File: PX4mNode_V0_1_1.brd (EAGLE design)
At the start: 48.6 x 34.9 mm, 140 parts, among them J201 DF13C-6P-1.25V, J202 DF13C-6P-1.25V, J203 DF13C-6P-1.25V, J301 DF13C-4P-1.25V, J401 DF13C-7P-1.25V, J402 DF13-4P-1.25V, J403 DF13C-4P-1.25V, J404 DF13C-4P-1.25V, J405 DF13C-4P-1.25V, J801 DF13C-3P-1.25V, M3_MOUNT1101 MOUNT-HOLE3.1MM, M3_MOUNT1102 MOUNT-HOLE3.1MM, M3_MOUNT1103 MOUNT-HOLE3.1MM, M3_MOUNT1104 MOUNT-HOLE3.1MM, U101 STM32F4X7VX, U401 MAX3051, U402 MAX3051, X101 3.2x2.5 mm / 24 MHz / 15 ppm

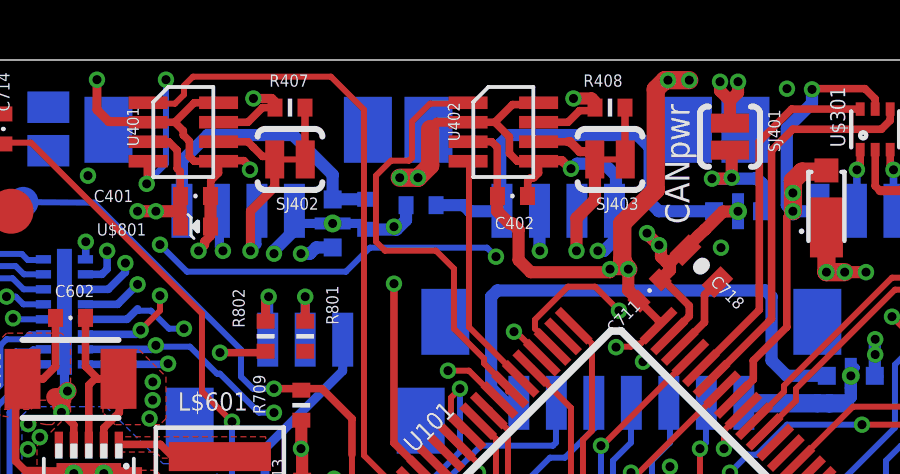
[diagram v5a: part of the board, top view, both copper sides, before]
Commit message: Stop mask removed from vias
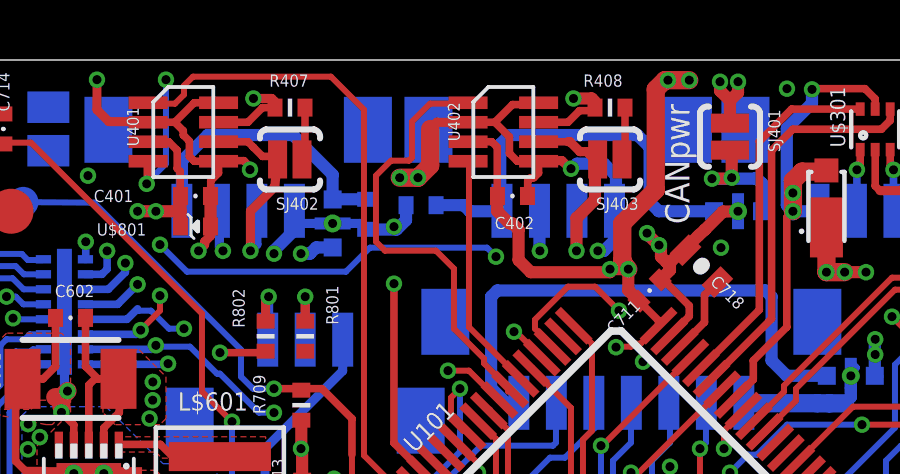
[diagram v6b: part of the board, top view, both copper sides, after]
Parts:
- SJ402, SJ403: value SOLDERJUMPERTRACE -> SOLDERJUMPERNC2; device SparkFun-Passives:SJ_2S-TRACE -> SparkFun-Passives:SJ_2S-NOTRACE
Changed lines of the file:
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@@
 <grid distance="0.1" unitdist="mm" unit="mm" style="dots" multiple="1" display="yes" altdistance="4" altunitdist="mil" altunit="mm"/>
 <layers>
-<layer number="1" name="Top" color="4" fill="1" visible="no" active="yes"/>
+<layer number="1" name="Top" color="4" fill="1" visible="yes" active="yes"/>
 <layer number="2" name="Ground" color="2" fill="10" visible="no" active="yes"/>
 <layer number="3" name="Horizontal" color="13" fill="15" visible="no" active="yes"/>
@@
 <layer number="13" name="Route13" color="4" fill="5" visible="no" active="no"/>
 <layer number="14" name="Vertical" color="14" fill="15" visible="no" active="yes"/>
-<layer number="15" name="Power" color="11" fill="15" visible="yes" active="yes"/>
-<layer number="16" name="Bottom" color="1" fill="1" visible="no" active="yes"/>
+<layer number="15" name="Power" color="11" fill="15" visible="no" active="yes"/>
+<layer number="16" name="Bottom" color="1" fill="1" visible="yes" active="yes"/>
 <layer number="17" name="Pads" color="2" fill="1" visible="yes" active="yes"/>
 <layer number="18" name="Vias" color="2" fill="1" visible="yes" active="yes"/>
-<layer number="19" name="Unrouted" color="14" fill="1" visible="yes" active="yes"/>
+<layer number="19" name="Unrouted" color="14" fill="1" visible="no" active="yes"/>
 <layer number="20" name="Dimension" color="15" fill="1" visible="yes" active="yes"/>
 <layer number="21" name="tPlace" color="7" fill="1" visible="yes" active="yes"/>
@@
 <layer number="27" name="tValues" color="7" fill="1" visible="no" active="yes"/>
 <layer number="28" name="bValues" color="7" fill="1" visible="no" active="yes"/>
-<layer number="29" name="tStop" color="7" fill="3" visible="no" active="yes"/>
+<layer number="29" name="tStop" color="7" fill="3" visible="yes" active="yes"/>
 <layer number="30" name="bStop" color="7" fill="6" visible="no" active="yes"/>
-<layer number="31" name="tCream" color="7" fill="4" visible="no" active="yes"/>
+<layer number="31" name="tCream" color="7" fill="4" visible="yes" active="yes"/>
 <layer number="32" name="bCream" color="7" fill="5" visible="no" active="yes"/>
 <layer number="33" name="tFinish" color="6" fill="3" visible="no" active="yes"/>
@@
 <param name="mlMinCreamFrame" value="0mil"/>
 <param name="mlMaxCreamFrame" value="0.2mm"/>
-<param name="mlViaStopLimit" value="0mil"/>
+<param name="mlViaStopLimit" value="0.31mm"/>
 <param name="srRoundness" value="0"/>
 <param name="srMinRoundness" value="0mil"/>
@@
 </element>
 <element name="L402" library="PX4lite" package="DFN16-THIN" value="NUF8402MN" x="49.9872" y="23.5712" rot="MR90"/>
-<element name="SJ403" library="SparkFun-Passives" package="SJ_2S-TRACE" value="SOLDERJUMPERTRACE" x="38.2016" y="34.3408" rot="R180"/>
+<element name="SJ403" library="SparkFun-Passives" package="SJ_2S-NOTRACE" value="SOLDERJUMPERNC2" x="38.2016" y="34.3408" rot="R180"/>
 <element name="J$401" library="PX4lite" package="HEADER_3X01_SMD_H_BOARD_EDGE_SHORT" value="HEADER-3X1BOARDEDGE-SHORT" x="45.6" y="3.9624" smashed="yes" rot="R180">
 <attribute name="NAME" x="52.0324" y="4.19" size="0.6096" layer="25" font="vector" ratio="15" rot="R180"/>
@@
 <attribute name="PARTNO" value="PESD0402-140" x="34.9504" y="34.7472" size="1.778" layer="28" rot="MR270" display="off"/>
 </element>
-<element name="SJ402" library="SparkFun-Passives" package="SJ_2S-TRACE" value="SOLDERJUMPERTRACE" x="27.5336" y="34.3408" rot="R180"/>
+<element name="SJ402" library="SparkFun-Passives" package="SJ_2S-NOTRACE" value="SOLDERJUMPERNC2" x="27.5336" y="34.3408" rot="R180"/>
 <element name="U$501" library="PX4lite" package="16LGA-3X3" value="MAX21100" x="49.276" y="9.7536" smashed="yes">
 <attribute name="NAME" x="48.376" y="7.2536" size="0.5" layer="25" font="vector" ratio="15"/>
@@
 <wire x1="37.084" y1="32.384" x2="37.7" y2="33" width="0.4064" layer="1"/>
 <wire x1="37.7" y1="33" x2="37.7" y2="34.3344" width="0.4064" layer="1"/>
-<wire x1="37.7" y1="34.3344" x2="37.6936" y2="34.3408" width="0.4064" layer="1"/>
+<wire x1="37.7" y1="34.3344" x2="37.7889" y2="34.3408" width="0.4064" layer="1"/>
 <wire x1="36.7994" y1="34.9302" x2="36.8698" y2="34.9302" width="0.3048" layer="1"/>
 <wire x1="36.8698" y1="34.9302" x2="37.2" y2="34.6" width="0.3048" layer="1"/>
 <wire x1="37.2" y1="34.6" x2="37.4344" y2="34.6" width="0.3048" layer="1"/>
-<wire x1="37.5344" y1="34.5" x2="37.6936" y2="34.3408" width="0.3048" layer="1"/>
+<wire x1="37.5344" y1="34.5" x2="37.7889" y2="34.3408" width="0.3048" layer="1"/>
 <wire x1="37.4344" y1="34.6" x2="37.5344" y2="34.5" width="0.3048" layer="1"/>
 </signal>
@@
 <vertex x="42.3" y="32.2"/>
 <vertex x="43.7" y="32.2"/>
-<vertex x="43.7" y="32.2"/>
 <vertex x="45.7" y="32.2"/>
 <vertex x="46.8" y="31.1"/>
@@
 <contactref element="SJ403" pad="1"/>
 <wire x1="38.7016" y1="36.068" x2="38.7016" y2="34.3488" width="0.254" layer="1"/>
-<wire x1="38.7016" y1="34.3488" x2="38.7096" y2="34.3408" width="0.254" layer="1"/>
+<wire x1="38.7016" y1="34.3488" x2="38.6025" y2="34.3408" width="0.254" layer="1"/>
 </signal>
 <signal name="N$28" class="1">
@@
 <contactref element="R407" pad="P$2"/>
 <contactref element="SJ402" pad="1"/>
-<wire x1="28.0416" y1="34.3408" x2="28.0336" y2="34.3488" width="0.254" layer="1"/>
+<wire x1="27.9345" y1="34.3408" x2="28.0336" y2="34.3488" width="0.254" layer="1"/>
 <wire x1="28.0336" y1="34.3488" x2="28.0336" y2="36.068" width="0.254" layer="1"/>
 </signal>
@@
 <contactref element="J404" pad="P$3"/>
 <contactref element="SJ402" pad="2"/>
-<wire x1="27.0256" y1="34.3408" x2="26.924" y2="34.4424" width="0.254" layer="1"/>
+<wire x1="27.1209" y1="34.3408" x2="26.924" y2="34.4424" width="0.254" layer="1"/>
 <wire x1="26.924" y1="34.4424" x2="26.616" y2="34.4424" width="0.254" layer="1"/>
 <wire x1="26.616" y1="34.4424" x2="26.3144" y2="34.744" width="0.254" layer="1"/>
@@
 <wire x1="26.216" y1="31.2928" x2="26.216" y2="32.6168" width="0.3048" layer="1"/>
 <wire x1="26.216" y1="32.6168" x2="27.0256" y2="33.4264" width="0.3048" layer="1"/>
-<wire x1="27.0256" y1="33.4264" x2="27.0256" y2="34.3408" width="0.3048" layer="1"/>
+<wire x1="27.0256" y1="33.4264" x2="27.1209" y2="34.3408" width="0.3048" layer="1"/>
 </signal>
 <signal name="REGD">

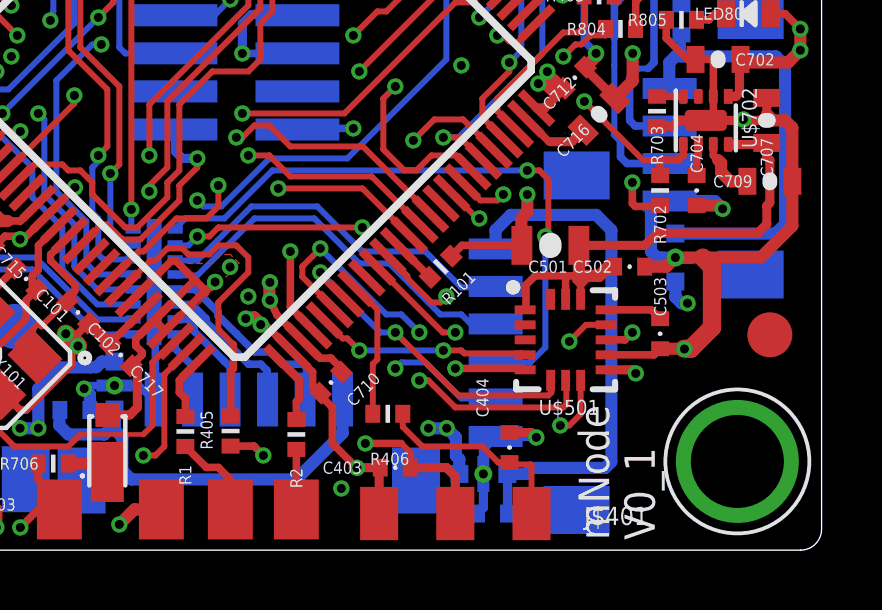
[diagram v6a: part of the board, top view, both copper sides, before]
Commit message: Tracking simplification around MAX21100
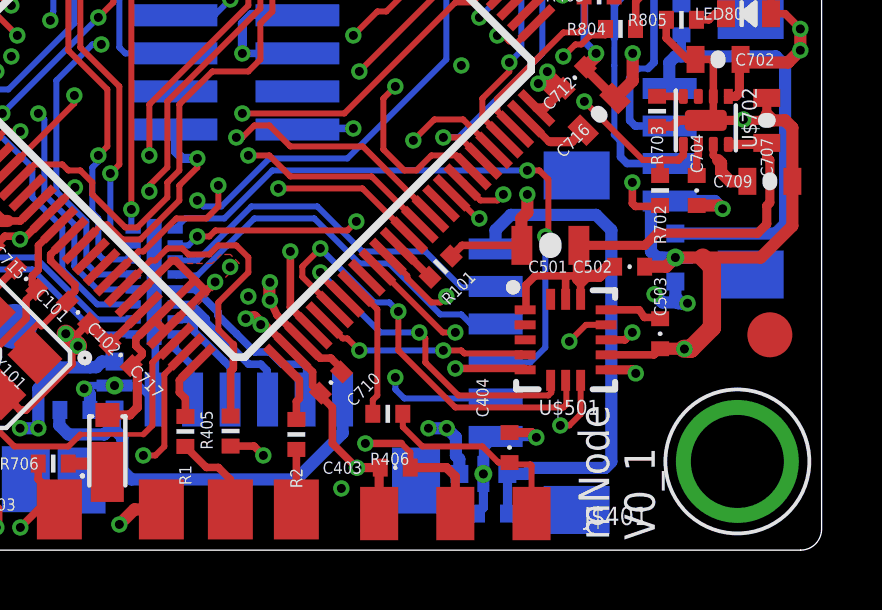
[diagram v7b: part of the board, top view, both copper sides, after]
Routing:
- net VDD_5V_PERIPH: track 68.8 -> 70.1 mm, vias 17 -> 18
- net SPI_INT_MISO: track 15.0 -> 14.8 mm, vias 3 -> 2
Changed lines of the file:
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@@
 <layer number="1" name="Top" color="4" fill="1" visible="yes" active="yes"/>
 <layer number="2" name="Ground" color="2" fill="10" visible="no" active="yes"/>
-<layer number="3" name="Horizontal" color="13" fill="15" visible="no" active="yes"/>
+<layer number="3" name="Horizontal" color="13" fill="15" visible="yes" active="yes"/>
 <layer number="4" name="Route4" color="1" fill="4" visible="no" active="no"/>
 <layer number="5" name="Route5" color="4" fill="4" visible="no" active="no"/>
@@
 <layer number="12" name="Route12" color="1" fill="5" visible="no" active="no"/>
 <layer number="13" name="Route13" color="4" fill="5" visible="no" active="no"/>
-<layer number="14" name="Vertical" color="14" fill="15" visible="no" active="yes"/>
-<layer number="15" name="Power" color="11" fill="15" visible="no" active="yes"/>
+<layer number="14" name="Vertical" color="14" fill="15" visible="yes" active="yes"/>
+<layer number="15" name="Power" color="11" fill="15" visible="yes" active="yes"/>
 <layer number="16" name="Bottom" color="1" fill="1" visible="yes" active="yes"/>
 <layer number="17" name="Pads" color="2" fill="1" visible="yes" active="yes"/>
 <layer number="18" name="Vias" color="2" fill="1" visible="yes" active="yes"/>
-<layer number="19" name="Unrouted" color="14" fill="1" visible="no" active="yes"/>
+<layer number="19" name="Unrouted" color="14" fill="1" visible="yes" active="yes"/>
 <layer number="20" name="Dimension" color="15" fill="1" visible="yes" active="yes"/>
 <layer number="21" name="tPlace" color="7" fill="1" visible="yes" active="yes"/>
@@
 <layer number="29" name="tStop" color="7" fill="3" visible="yes" active="yes"/>
 <layer number="30" name="bStop" color="7" fill="6" visible="no" active="yes"/>
-<layer number="31" name="tCream" color="7" fill="4" visible="yes" active="yes"/>
+<layer number="31" name="tCream" color="7" fill="4" visible="no" active="yes"/>
 <layer number="32" name="bCream" color="7" fill="5" visible="no" active="yes"/>
 <layer number="33" name="tFinish" color="6" fill="3" visible="no" active="yes"/>
@@
 <wire x1="37" y1="13.2" x2="36.7" y2="12.9" width="0.2" layer="16"/>
 <wire x1="37.4" y1="13.2" x2="37" y2="13.2" width="0.2" layer="1"/>
-<wire x1="37.7" y1="13.5" x2="37.4" y2="13.2" width="0.2" layer="1"/>
-<wire x1="42.5" y1="13.5" x2="37.7" y2="13.5" width="0.2" layer="1"/>
-<wire x1="43" y1="13" x2="42.5" y2="13.5" width="0.2" layer="14"/>
-<wire x1="43" y1="9.4" x2="43" y2="13" width="0.2" layer="14"/>
-<wire x1="43.6" y1="8.8" x2="43" y2="9.4" width="0.2" layer="14"/>
-<wire x1="43.8" y1="9" x2="43.6" y2="8.8" width="0.2" layer="16"/>
-<wire x1="44.6" y1="9" x2="43.8" y2="9" width="0.2" layer="16"/>
-<wire x1="45.8" y1="7.8" x2="44.6" y2="9" width="0.2" layer="16"/>
-<wire x1="46.9" y1="7.8" x2="45.8" y2="7.8" width="0.2" layer="16"/>
+<wire x1="37.6" y1="13.4" x2="37.4" y2="13.2" width="0.2" layer="1"/>
+<wire x1="42.3" y1="13.7" x2="42" y2="13.4" width="0.2" layer="1"/>
+<wire x1="42" y1="13.4" x2="37.6" y2="13.4" width="0.2" layer="1"/>
+<wire x1="43.1" y1="12.9" x2="42.3" y2="13.7" width="0.2" layer="14"/>
+<wire x1="43.1" y1="9" x2="43.1" y2="12.9" width="0.2" layer="14"/>
+<wire x1="43.6" y1="8.5" x2="43.1" y2="9" width="0.2" layer="14"/>
+<wire x1="43.6" y1="8.1" x2="43.6" y2="8.5" width="0.2" layer="16"/>
+<wire x1="43.9" y1="7.8" x2="43.6" y2="8.1" width="0.2" layer="16"/>
+<wire x1="46.9" y1="7.8" x2="43.9" y2="7.8" width="0.2" layer="16"/>
 <wire x1="36.3" y1="12.9" x2="36.26" y2="12.934" width="0.2" layer="16"/>
 <wire x1="46.9" y1="7.8" x2="46.9456" y2="7.7834" width="0.2" layer="16"/>
 <via x="37" y="13.2" extent="1-16" drill="0.3" diameter="0.55"/>
-<via x="42.5" y="13.5" extent="1-16" drill="0.3" diameter="0.55"/>
-<via x="43.6" y="8.8" extent="1-16" drill="0.3" diameter="0.55"/>
+<via x="42.3" y="13.7" extent="1-16" drill="0.3" diameter="0.55"/>
+<via x="43.6" y="8.5" extent="1-16" drill="0.3" diameter="0.55"/>
 </signal>
 <signal name="SDIO_D0">
@@
 <wire x1="39.7" y1="9.3" x2="38.5" y2="9.3" width="0.2" layer="3"/>
 <wire x1="40.1" y1="12.7" x2="40.5" y2="12.3" width="0.2" layer="3"/>
-<wire x1="40.5" y1="12.3" x2="40.5" y2="11.8" width="0.2" layer="3"/>
-<wire x1="40.5" y1="11.8" x2="40.8" y2="11.5" width="0.2" layer="3"/>
-<wire x1="40.8" y1="11.5" x2="40.8" y2="10.4" width="0.2" layer="3"/>
-<wire x1="40.8" y1="10.4" x2="39.7" y2="9.3" width="0.2" layer="3"/>
+<wire x1="40.5" y1="12.3" x2="40.5" y2="10.2" width="0.2" layer="3"/>
+<wire x1="40.5" y1="10.2" x2="39.7" y2="9.3" width="0.2" layer="3"/>
 <wire x1="19.8" y1="11.8" x2="19.7104" y2="11.8872" width="0.2" layer="3"/>
 <via x="40.1" y="12.7" extent="1-16" drill="0.3" diameter="0.55"/>
@@
 <wire x1="49.2" y1="7.5" x2="49.3" y2="7.6" width="0.2" layer="1"/>
 <wire x1="45.6" y1="7.5" x2="49.2" y2="7.5" width="0.2" layer="1"/>
-<wire x1="44.7" y1="8.4" x2="45.6" y2="7.5" width="0.2" layer="1"/>
-<wire x1="44.4" y1="8.4" x2="44.7" y2="8.4" width="0.2" layer="1"/>
-<wire x1="44.4" y1="10" x2="44.4" y2="8.4" width="0.2" layer="14"/>
-<wire x1="43.8" y1="10.6" x2="44.4" y2="10" width="0.2" layer="16"/>
-<wire x1="43.3" y1="10.6" x2="43.8" y2="10.6" width="0.2" layer="16"/>
-<wire x1="41.1" y1="12.8" x2="43.3" y2="10.6" width="0.2" layer="16"/>
+<wire x1="43.4" y1="11" x2="43.7" y2="10.7" width="0.2" layer="16"/>
+<wire x1="42.9" y1="11" x2="43.4" y2="11" width="0.2" layer="16"/>
+<wire x1="41.1" y1="12.8" x2="42.9" y2="11" width="0.2" layer="16"/>
 <wire x1="40.5" y1="12.2" x2="41.1" y2="12.8" width="0.2" layer="1"/>
 <wire x1="40.5" y1="11.85265" x2="40.5" y2="12.2" width="0.2" layer="1"/>
 <wire x1="49.3" y1="8.4" x2="49.276" y2="8.4036" width="0.2" layer="1"/>
 <wire x1="41.5" y1="10.8" x2="41.586778125" y2="10.765871875" width="0.2" layer="1"/>
-<via x="44.4" y="8.4" extent="1-16" drill="0.3" diameter="0.55"/>
-<via x="44.4" y="10" extent="1-16" drill="0.3" diameter="0.55"/>
+<via x="43.7" y="10.7" extent="1-16" drill="0.3" diameter="0.55"/>
 <via x="41.1" y="12.8" extent="1-16" drill="0.3" diameter="0.55"/>
 <wire x1="40.5" y1="11.85265" x2="41.586778125" y2="10.765871875" width="0.2" layer="1"/>
+<wire x1="45.6" y1="7.5" x2="43.7" y2="9.4" width="0.2" layer="1"/>
+<wire x1="43.7" y1="9.4" x2="43.7" y2="10.7" width="0.2" layer="1"/>
 </signal>
 <signal name="SPI_INT_MOSI">
@@
 <wire x1="48.7" y1="7.9" x2="48.8" y2="8" width="0.2" layer="1"/>
 <wire x1="45.7" y1="7.9" x2="48.7" y2="7.9" width="0.2" layer="1"/>
-<wire x1="43.6" y1="10" x2="45.7" y2="7.9" width="0.2" layer="1"/>
-<wire x1="43.1" y1="10" x2="43.6" y2="10" width="0.2" layer="16"/>
+<wire x1="44.4" y1="10" x2="44.6" y2="9.8" width="0.2" layer="1"/>
+<wire x1="44.6" y1="9.8" x2="44.6" y2="9" width="0.2" layer="1"/>
+<wire x1="44.6" y1="9" x2="45.7" y2="7.9" width="0.2" layer="1"/>
+<wire x1="43.1" y1="10" x2="44.4" y2="10" width="0.2" layer="16"/>
 <wire x1="41.1" y1="12" x2="43.1" y2="10" width="0.2" layer="16"/>
 <wire x1="41.1" y1="11.9" x2="41.1" y2="12" width="0.2" layer="1"/>
@@
 <wire x1="48.8" y1="8.4" x2="48.776" y2="8.4036" width="0.2" layer="1"/>
 <wire x1="41.9" y1="11.1" x2="41.94033125" y2="11.119425" width="0.2" layer="1"/>
-<via x="43.6" y="10" extent="1-16" drill="0.3" diameter="0.55"/>
+<via x="44.4" y="10" extent="1-16" drill="0.3" diameter="0.55"/>
 <via x="41.1" y="12" extent="1-16" drill="0.3" diameter="0.55"/>
 </signal>
@@
 <wire x1="42.3" y1="11.5" x2="42.293884375" y2="11.472978125" width="0.2" layer="1"/>
 <wire x1="43" y1="10.7668625" x2="42.293884375" y2="11.472978125" width="0.2" layer="1"/>
-<wire x1="43" y1="10.7668625" x2="43" y2="9.1" width="0.2" layer="1"/>
-<wire x1="43" y1="9.1" x2="42.848" y2="8.948" width="0.2" layer="1"/>
-<wire x1="42.848" y1="8.948" x2="42.848" y2="7.288" width="0.2" layer="1"/>
+<wire x1="43" y1="10.7668625" x2="43" y2="7.9" width="0.2" layer="1"/>
+<wire x1="43" y1="7.9" x2="42.848" y2="7.748" width="0.2" layer="1"/>
+<wire x1="42.848" y1="7.748" x2="42.848" y2="7.288" width="0.2" layer="1"/>
 </signal>
 <signal name="N$68">
@@
 <contactref element="C503" pad="P$1"/>
 <contactref element="U$501" pad="13"/>
-<wire x1="50.626" y1="10.7536" x2="52.1288" y2="10.7536" width="0.254" layer="1"/>
-<wire x1="52.1288" y1="10.7536" x2="52.4256" y2="10.4568" width="0.254" layer="1"/>
+<wire x1="50.626" y1="10.7536" x2="51.7288" y2="10.7536" width="0.254" layer="1"/>
+<wire x1="51.7288" y1="10.7536" x2="51.9" y2="10.5" width="0.254" layer="1"/>
+<wire x1="51.9" y1="10.5" x2="52.3824" y2="10.5" width="0.254" layer="1"/>
+<wire x1="52.3824" y1="10.5" x2="52.4256" y2="10.4568" width="0.254" layer="1"/>
 </signal>
 <signal name="VDD_SERVO_SENS">
@@
 <wire x1="21.4" y1="9.7" x2="21.336" y2="9.6504" width="0.254" layer="15"/>
 <wire x1="21.4" y1="9.7" x2="21.6408" y2="9.5504" width="0.254" layer="15"/>
+<via x="52.24" y="11.2728" extent="1-16" drill="0.3" diameter="0.55"/>
+<wire x1="52.2272" y1="11.2728" x2="52.5" y2="11" width="0.4064" layer="16"/>
+<wire x1="52.5" y1="11" x2="53" y2="11" width="0.4064" layer="16"/>
+<wire x1="52.2" y1="11.3" x2="52.2272" y2="11.2728" width="0.4064" layer="16"/>
+<wire x1="52.2272" y1="11.2728" x2="52.24" y2="11.2728" width="0.4064" layer="16"/>
+<wire x1="53" y1="11" x2="53.0272" y2="10.9728" width="0.4064" layer="16"/>
+<wire x1="53.0272" y1="10.9728" x2="53.34" y2="10.9728" width="0.4064" layer="16"/>
 </signal>
 <signal name="VDD_3V3_PERIPH" class="1">
